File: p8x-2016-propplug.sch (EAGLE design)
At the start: 23 parts, among them CN1 USB_B, IC1 PIC18F24J50-I/P

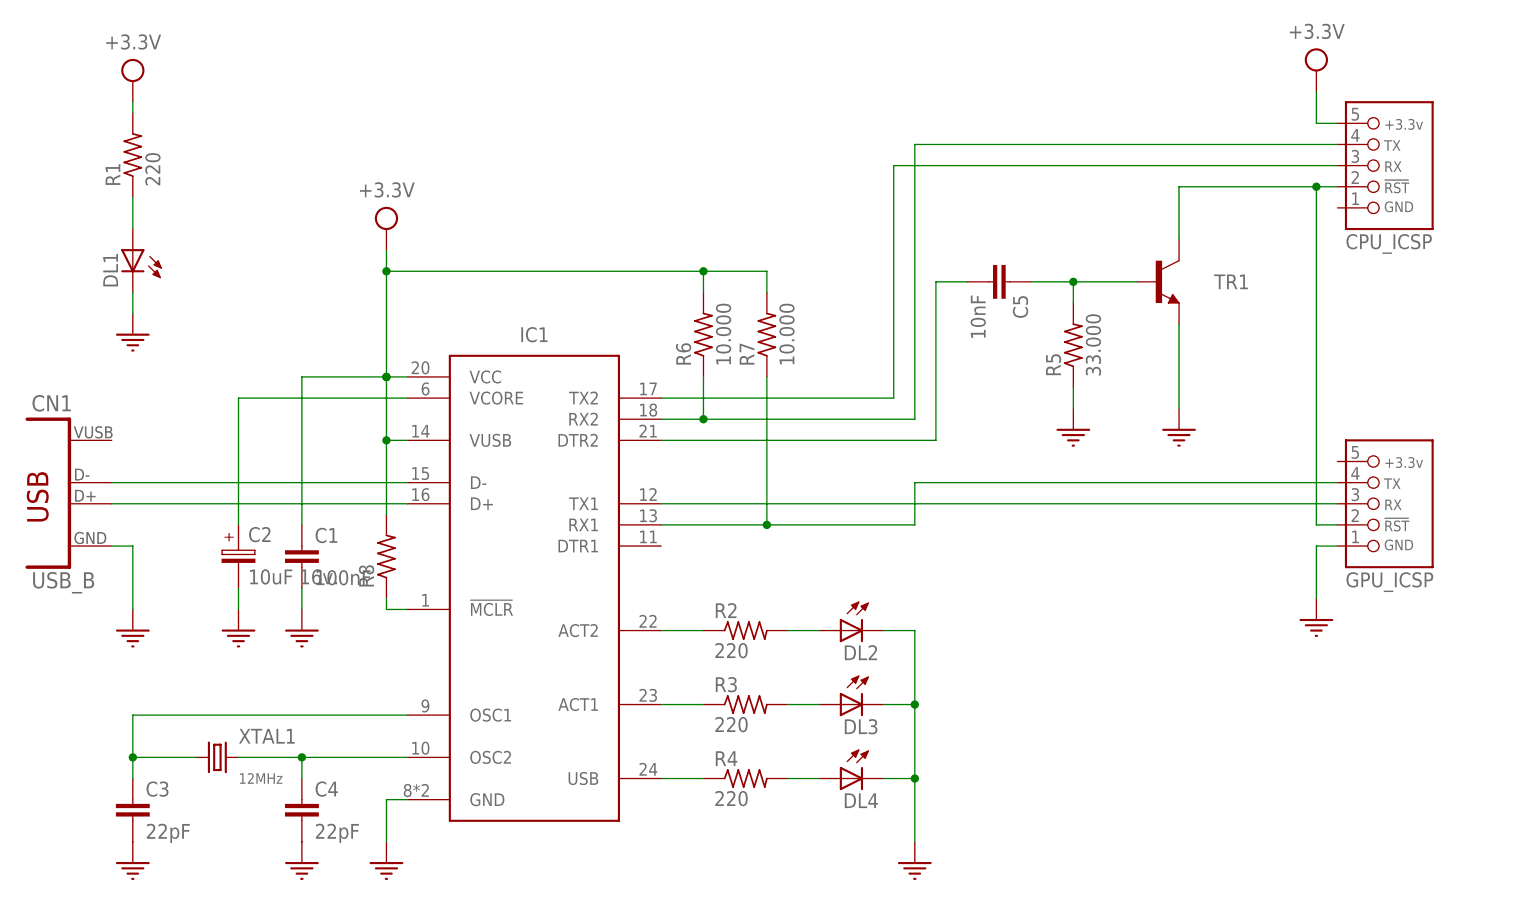
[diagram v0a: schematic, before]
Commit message: Updates and fixes for PIC18F24J50
 * Fixed configuration bits
 * TX lines configured as open-drain and added pull-up resistors
 * UART initialization moved at startup
 * Speed optimizations
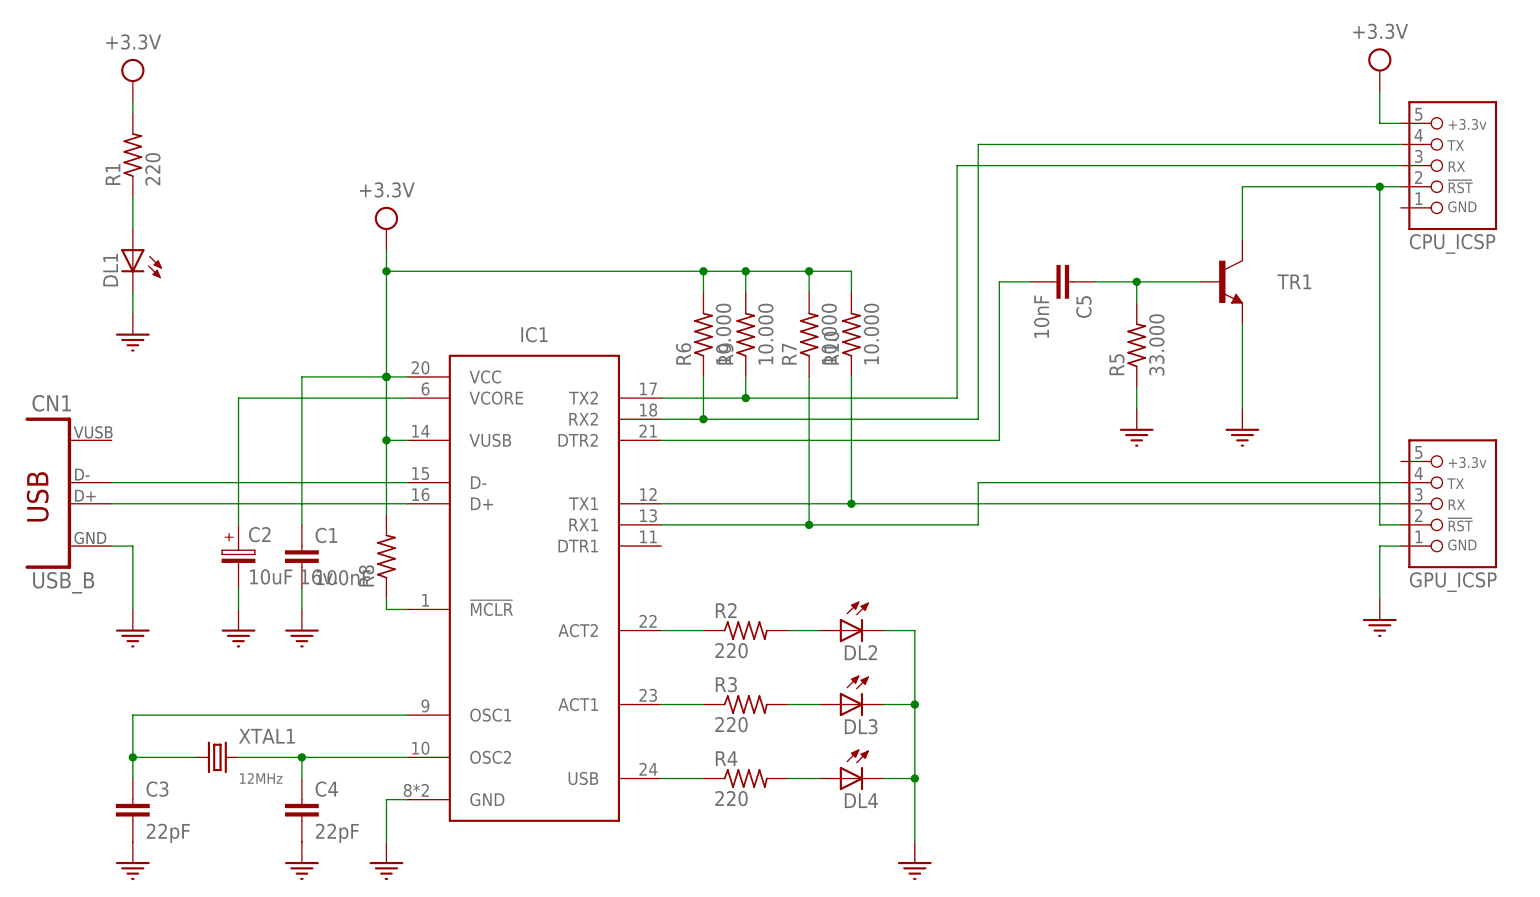
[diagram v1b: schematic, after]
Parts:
- added R10, R9: 10.000, p8x-2016:R-1/4W
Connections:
- net +3.3V: now also R10.2, R9.2
- net TX1: now also R9.1
- net TX2: now also R10.1
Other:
- moved on the sheet: C5, CPU_ICSP, GPU_ICSP, R5, R7, TR1
